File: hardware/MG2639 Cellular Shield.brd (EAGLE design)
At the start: 53.3 x 73.7 mm, 50 parts, among them J1 SIMHOLDER, Q1 MMBT2222A, Q2 MMBT2222A, U1 TXB0108, U2 SPX29302, U4 ARDUINO_R3_SHIELDNOLABELS, U5 MG2639V3

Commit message: Corrected +/- on battery connector
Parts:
- C10, C11, C3: device SparkFun:0603-CAP -> SparkFun-Capacitors:0603-CAP
- renumbered JP3 to JP5
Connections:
- net 3.8V: now also JP5.2; no longer JP5.1
- net GND: now also JP5.1; no longer JP5.2
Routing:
- net 3.8V: track 69.5 -> 71.8 mm
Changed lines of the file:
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@@
 <layer number="44" name="Drills" color="7" fill="1" visible="no" active="yes"/>
 <layer number="45" name="Holes" color="7" fill="1" visible="yes" active="yes"/>
-<layer number="46" name="Milling" color="3" fill="1" visible="yes" active="yes"/>
+<layer number="46" name="Milling" color="3" fill="1" visible="no" active="yes"/>
 <layer number="47" name="Measures" color="7" fill="1" visible="no" active="yes"/>
 <layer number="48" name="Document" color="7" fill="1" visible="no" active="yes"/>
-<layer number="49" name="Reference" color="7" fill="1" visible="yes" active="yes"/>
+<layer number="49" name="Reference" color="7" fill="1" visible="no" active="yes"/>
 <layer number="50" name="dxf" color="7" fill="1" visible="no" active="yes"/>
 <layer number="51" name="tDocu" color="6" fill="1" visible="yes" active="yes"/>
@@
 </autorouter>
 <elements>
-<element name="C3" library="SparkFun" package="0603-CAP" value="0.1uF" x="40.64" y="29.21" rot="R180"/>
+<element name="C3" library="SparkFun-Capacitors" package="0603-CAP" value="0.1uF" x="40.64" y="29.21" rot="R180">
+<attribute name="PROD_ID" value="CAP-00810" x="40.64" y="29.21" size="1.778" layer="27" rot="R180" display="off"/>
+<attribute name="VALUE" value="0.1uF" x="40.64" y="29.21" size="1.778" layer="27" rot="R180" display="off"/>
+</element>
 <element name="U$1" library="SparkFun" package="CREATIVE_COMMONS" value="CREATIVE_COMMONS" x="20.32" y="-16.51" smashed="yes"/>
 <element name="U5" library="MG2639" package="MG2639" value="MG2639V3" x="19.05" y="24.13"/>
@@
 <attribute name="PROD_ID" value="CAP-09824" x="44.45" y="20.32" size="1.778" layer="27" font="vector" ratio="15" display="off"/>
 </element>
-<element name="U2" library="SparkFun-PowerIC" package="Q5-DD_SPX29300" value="SPX29302" x="43.18" y="41.91"/>
+<element name="U2" library="SparkFun-PowerIC" package="Q5-DD_SPX29300" value="SPX29302" x="43.18" y="41.91">
+<attribute name="PROD_ID" value="VREG-08337" x="43.18" y="41.91" size="1.778" layer="27" display="off"/>
+</element>
 <element name="C2" library="SparkFun-Capacitors" package="1210" value="10uF" x="36.83" y="33.02" rot="R90">
 <attribute name="PROD_ID" value="CAP-09824" x="36.83" y="33.02" size="1.778" layer="27" font="vector" ratio="15" rot="R90" display="off"/>
@@
 <element name="LOGO1" library="SparkFun-Aesthetics" package="SFE_LOGO_NAME_FLAME_.1" value="SFE_LOGO_NAME_FLAME.1_INCH" x="24.765" y="41.275"/>
 <element name="LOGO2" library="SparkFun-Aesthetics" package="OSHW-LOGO-S" value="OSHW-LOGOS" x="35.56" y="24.003"/>
-<element name="S2" library="SparkFun-Electromechanical" package="TACTILE-SWITCH-SMD" value="BOOT" x="36.83" y="12.7" rot="R180"/>
+<element name="S2" library="SparkFun-Electromechanical" package="TACTILE-SWITCH-SMD" value="BOOT" x="36.83" y="12.7" rot="R180">
+<attribute name="PROD_ID" value="SWCH-08247" x="36.83" y="12.7" size="1.778" layer="27" rot="R180" display="off"/>
+</element>
 <element name="J1" library="SparkFun-Connectors" package="SIMHOLDER" value="SIMHOLDER" x="24.13" y="64.77" rot="R180">
 <attribute name="PROD_ID" value="CONN-08536" x="24.13" y="64.77" size="1.778" layer="27" rot="R180" display="off"/>
@@
 </element>
 <element name="SJ1" library="SparkFun-Passives" package="PAD-JUMPER-2-NC_BY_TRACE_YES_SILK" value="" x="24.13" y="45.085" rot="R90"/>
-<element name="BAT1" library="SparkFun-Electromechanical" package="BATTCON_12MM" value="20mm coincell" x="46.99" y="63.5" rot="R270"/>
+<element name="BAT1" library="SparkFun-Electromechanical" package="BATTCON_12MM" value="20mm coincell" x="46.99" y="63.5" rot="R270">
+<attribute name="PROD_ID" value="BATT-08044" x="46.99" y="63.5" size="1.778" layer="27" rot="R270" display="off"/>
+</element>
 <element name="SJ2" library="SparkFun-Passives" package="PAD-JUMPER-2-NC_BY_TRACE_YES_SILK" value="" x="22.86" y="6.35"/>
-<element name="S3" library="SparkFun-Electromechanical" package="TACTILE-SWITCH-SMD" value="BOOT" x="36.83" y="5.08"/>
+<element name="S3" library="SparkFun-Electromechanical" package="TACTILE-SWITCH-SMD" value="BOOT" x="36.83" y="5.08">
+<attribute name="PROD_ID" value="SWCH-08247" x="36.83" y="5.08" size="1.778" layer="27" display="off"/>
+</element>
 <element name="R8" library="SparkFun-Resistors" package="0603-RES" value="1K" x="17.78" y="45.72" rot="R90">
 <attribute name="PROD_ID" value="RES-07856" x="17.78" y="45.72" size="1.778" layer="27" font="vector" ratio="15" rot="R90" display="off"/>
@@
 <element name="SJ3" library="SparkFun-Passives" package="PAD-JUMPER-3-2OF3_NC_BY_PASTE_YES_SILK_FULL_BOX" value="" x="7.62" y="48.26" rot="R90"/>
 <element name="SJ4" library="SparkFun-Passives" package="PAD-JUMPER-3-2OF3_NC_BY_PASTE_YES_SILK_FULL_BOX" value="" x="7.62" y="52.07" rot="R90"/>
-<element name="U1" library="Testing" package="UFDFN-20" value="TXB0108" x="12.7" y="45.72" rot="R90"/>
+<element name="U1" library="Testing" package="UFDFN-20" value="TXB0108" x="12.7" y="45.72" rot="R90">
+<attribute name="PROD_ID" value="IC-12292" x="12.7" y="45.72" size="1.778" layer="27" rot="R90" display="off"/>
+</element>
 <element name="SJ5" library="SparkFun-Passives" package="PAD-JUMPER-3-2OF3_NC_BY_PASTE_YES_SILK_FULL_BOX" value="" x="12.7" y="49.53"/>
 <element name="JP4" library="SparkFun-Connectors" package="1X03" value="" x="2.54" y="58.42" rot="MR90"/>
 <element name="JP2" library="SparkFun-Connectors" package="1X07" value="" x="19.05" y="1.27" rot="R180"/>
-<element name="C10" library="SparkFun" package="0603-CAP" value="0.1uF" x="13.97" y="53.34" rot="R90"/>
-<element name="C11" library="SparkFun" package="0603-CAP" value="0.1uF" x="11.43" y="53.34" rot="R90"/>
+<element name="C10" library="SparkFun-Capacitors" package="0603-CAP" value="0.1uF" x="13.97" y="53.34" rot="R90">
+<attribute name="PROD_ID" value="CAP-00810" x="13.97" y="53.34" size="1.778" layer="27" rot="R90" display="off"/>
+<attribute name="VALUE" value="0.1uF" x="13.97" y="53.34" size="1.778" layer="27" rot="R90" display="off"/>
+</element>
+<element name="C11" library="SparkFun-Capacitors" package="0603-CAP" value="0.1uF" x="11.43" y="53.34" rot="R90">
+<attribute name="PROD_ID" value="CAP-00810" x="11.43" y="53.34" size="1.778" layer="27" rot="R90" display="off"/>
+<attribute name="VALUE" value="0.1uF" x="11.43" y="53.34" size="1.778" layer="27" rot="R90" display="off"/>
+</element>
 <element name="D3" library="SparkFun-LED" package="LED-1206" value="GREEN" x="20.32" y="45.72" rot="R90">
 <attribute name="PROD_ID" value="DIO-00862" x="20.32" y="45.72" size="1.778" layer="27" font="vector" ratio="15" rot="R90" display="off"/>
@@
 <attribute name="PROD_ID" value="RES-07856" x="45.72" y="29.21" size="1.778" layer="27" font="vector" ratio="15" display="off"/>
 </element>
-<element name="R2" library="SparkFun-Resistors" package="0603-RES" value="4.7K" x="25.4" y="6.35" rot="R90"/>
-<element name="R13" library="SparkFun-Resistors" package="0603-RES" value="4.7K" x="5.08" y="43.18" rot="R90"/>
+<element name="R2" library="SparkFun-Resistors" package="0603-RES" value="4.7K" x="25.4" y="6.35" rot="R90">
+<attribute name="PROD_ID" value="RES-07857" x="25.4" y="6.35" size="1.778" layer="27" rot="R90" display="off"/>
+<attribute name="VALUE" value="4.7K" x="25.4" y="6.35" size="1.778" layer="27" rot="R90" display="off"/>
+</element>
+<element name="R13" library="SparkFun-Resistors" package="0603-RES" value="4.7K" x="5.08" y="43.18" rot="R90">
+<attribute name="PROD_ID" value="RES-07857" x="5.08" y="43.18" size="1.778" layer="27" rot="R90" display="off"/>
+<attribute name="VALUE" value="4.7K" x="5.08" y="43.18" size="1.778" layer="27" rot="R90" display="off"/>
+</element>
 <element name="U$2" library="SparkFun-RF" package="SMA_BULKHEAD" value="SMA_HOLE" x="40.767" y="53.975"/>
 <element name="LOGO3" library="SparkFun-Aesthetics" package="SFE_LOGO_NAME_FLAME_.2" value="SFE_LOGO_NAME_FLAME.2_INCH" x="38.481" y="33.528" rot="MR0"/>
 <element name="SJ6" library="SparkFun-Passives" package="PAD-JUMPER-2-NC_BY_TRACE_YES_SILK" value="" x="43.18" y="29.21" rot="R270"/>
-<element name="JP3" library="SparkFun-Connectors" package="JST-2-PTH" value="LiPo" x="46.99" y="12.7" rot="R270">
-<attribute name="SKU" value="PRT-09914" x="46.99" y="12.7" size="1.016" layer="27" font="vector" ratio="15" rot="R270" display="off"/>
+<element name="JP5" library="SparkFun-Connectors" package="JST-2-PTH" value="LiPo" x="46.99" y="12.7" rot="R270">
+<attribute name="SKU" value="PRT-09914" x="46.99" y="12.7" size="1.778" layer="27" font="vector" ratio="15" rot="R270" display="off"/>
 </element>
 </elements>
@@
 <via x="21.082" y="40.64" extent="1-16" drill="0.508"/>
 <via x="20.32" y="35.56" extent="1-16" drill="0.508"/>
-<contactref element="JP3" pad="2"/>
+<contactref element="JP5" pad="1"/>
 </signal>
 <signal name="SIM_CLK">
@@
 <wire x1="35.56" y1="25.4" x2="34.29" y2="26.67" width="0.4572" layer="1"/>
 <contactref element="SJ6" pad="2"/>
-<contactref element="JP3" pad="1"/>
 <wire x1="43.18" y1="28.702" x2="43.18" y2="28.067" width="0.4572" layer="1"/>
 <wire x1="43.18" y1="28.067" x2="42.545" y2="27.432" width="0.4572" layer="1"/>
@@
 <wire x1="41.49" y1="27.471" x2="41.529" y2="27.432" width="0.4572" layer="1"/>
 <wire x1="42.85" y1="20.32" x2="42.85" y2="16.84" width="0.4572" layer="1"/>
-<wire x1="42.85" y1="16.84" x2="45.99" y2="13.7" width="0.4572" layer="1"/>
-<wire x1="46.99" y1="13.7" x2="45.99" y2="13.7" width="0.4572" layer="1"/>
+<contactref element="JP5" pad="2"/>
+<wire x1="42.85" y1="16.84" x2="44.45" y2="15.24" width="0.4572" layer="1"/>
+<wire x1="44.45" y1="15.24" x2="44.45" y2="12.7" width="0.4572" layer="1"/>
+<wire x1="46.99" y1="11.7" x2="45.45" y2="11.7" width="0.4572" layer="1"/>
+<wire x1="45.45" y1="11.7" x2="44.45" y2="12.7" width="0.4572" layer="1"/>
 </signal>
 <signal name="N$2">

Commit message: Prelim firmware. Works for certain features.
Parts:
- BAT1: value 20mm coincell -> 12mm coincell
- D2: value RED -> BLUE
- U4: value ARDUINO_R3_SHIELDNOLABELS -> ARDUINO_R3_SHIELD
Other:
- board text added: "+"
- board text added: "BATT"
- board text added: "N. Seidle"
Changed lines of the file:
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@@
 <layer number="37" name="tTest" color="7" fill="1" visible="no" active="yes"/>
 <layer number="38" name="bTest" color="7" fill="1" visible="no" active="yes"/>
-<layer number="39" name="tKeepout" color="4" fill="11" visible="no" active="yes"/>
-<layer number="40" name="bKeepout" color="1" fill="11" visible="no" active="yes"/>
+<layer number="39" name="tKeepout" color="4" fill="11" visible="yes" active="yes"/>
+<layer number="40" name="bKeepout" color="1" fill="11" visible="yes" active="yes"/>
 <layer number="41" name="tRestrict" color="4" fill="10" visible="no" active="yes"/>
 <layer number="42" name="bRestrict" color="1" fill="10" visible="no" active="yes"/>
@@
 <layer number="47" name="Measures" color="7" fill="1" visible="no" active="yes"/>
 <layer number="48" name="Document" color="7" fill="1" visible="no" active="yes"/>
-<layer number="49" name="Reference" color="7" fill="1" visible="no" active="yes"/>
+<layer number="49" name="Reference" color="7" fill="1" visible="yes" active="yes"/>
 <layer number="50" name="dxf" color="7" fill="1" visible="no" active="yes"/>
 <layer number="51" name="tDocu" color="6" fill="1" visible="yes" active="yes"/>
@@
 Batt</text>
 <text x="48.641" y="28.194" size="1.016" layer="21" font="vector" ratio="15" rot="R90">SJ6</text>
+<text x="48.387" y="10.795" size="1.778" layer="21" font="vector" ratio="15">+</text>
+<text x="48.387" y="12.827" size="1.778" layer="21" font="vector" ratio="15">-</text>
+<text x="46.99" y="16.002" size="1.27" layer="21" font="vector" ratio="15">BATT</text>
+<text x="52.07" y="-16.51" size="1.778" layer="27" font="vector" ratio="15">N. Seidle</text>
 </plain>
 <attributes>
@@
 <attribute name="PROD_ID" value="CAP-07890" x="43.18" y="25.4" size="1.778" layer="27" font="vector" ratio="15" rot="R180" display="off"/>
 </element>
-<element name="U4" library="SparkFun-Boards" package="UNO_R3_SHIELD_NOLABELS" value="ARDUINO_R3_SHIELDNOLABELS" x="0" y="0"/>
+<element name="U4" library="SparkFun-Boards" package="UNO_R3_SHIELD_NOLABELS" value="ARDUINO_R3_SHIELD" x="0" y="0"/>
 <element name="Q1" library="SparkFun-DiscreteSemi" package="SOT23-3" value="MMBT2222A" x="27.94" y="6.35" rot="R270">
 <attribute name="PROD_ID" value="TRANS-08049" x="27.94" y="6.35" size="1.778" layer="27" rot="R270" display="off"/>
@@
 </element>
 <element name="SJ1" library="SparkFun-Passives" package="PAD-JUMPER-2-NC_BY_TRACE_YES_SILK" value="" x="24.13" y="45.085" rot="R90"/>
-<element name="BAT1" library="SparkFun-Electromechanical" package="BATTCON_12MM" value="20mm coincell" x="46.99" y="63.5" rot="R270">
+<element name="BAT1" library="SparkFun-Electromechanical" package="BATTCON_12MM" value="12mm coincell" x="46.99" y="63.5" rot="R270">
 <attribute name="PROD_ID" value="BATT-08044" x="46.99" y="63.5" size="1.778" layer="27" rot="R270" display="off"/>
 </element>
@@
 <attribute name="PROD_ID" value="RES-07856" x="17.78" y="45.72" size="1.778" layer="27" font="vector" ratio="15" rot="R90" display="off"/>
 </element>
-<element name="D2" library="SparkFun-LED" package="LED-1206" value="RED" x="2.54" y="6.35" rot="R270">
-<attribute name="PROD_ID" value="DIO-00809" x="2.54" y="6.35" size="1.778" layer="27" font="vector" ratio="15" rot="R270" display="off"/>
+<element name="D2" library="SparkFun-LED" package="LED-1206" value="BLUE" x="2.54" y="6.35" rot="R270">
+<attribute name="PROD_ID" value="DIO-09911" x="2.54" y="6.35" size="1.778" layer="27" font="vector" ratio="15" rot="R270" display="off"/>
 </element>
 <element name="R9" library="SparkFun-Resistors" package="0603-RES" value="1K" x="5.08" y="10.16" rot="R270">

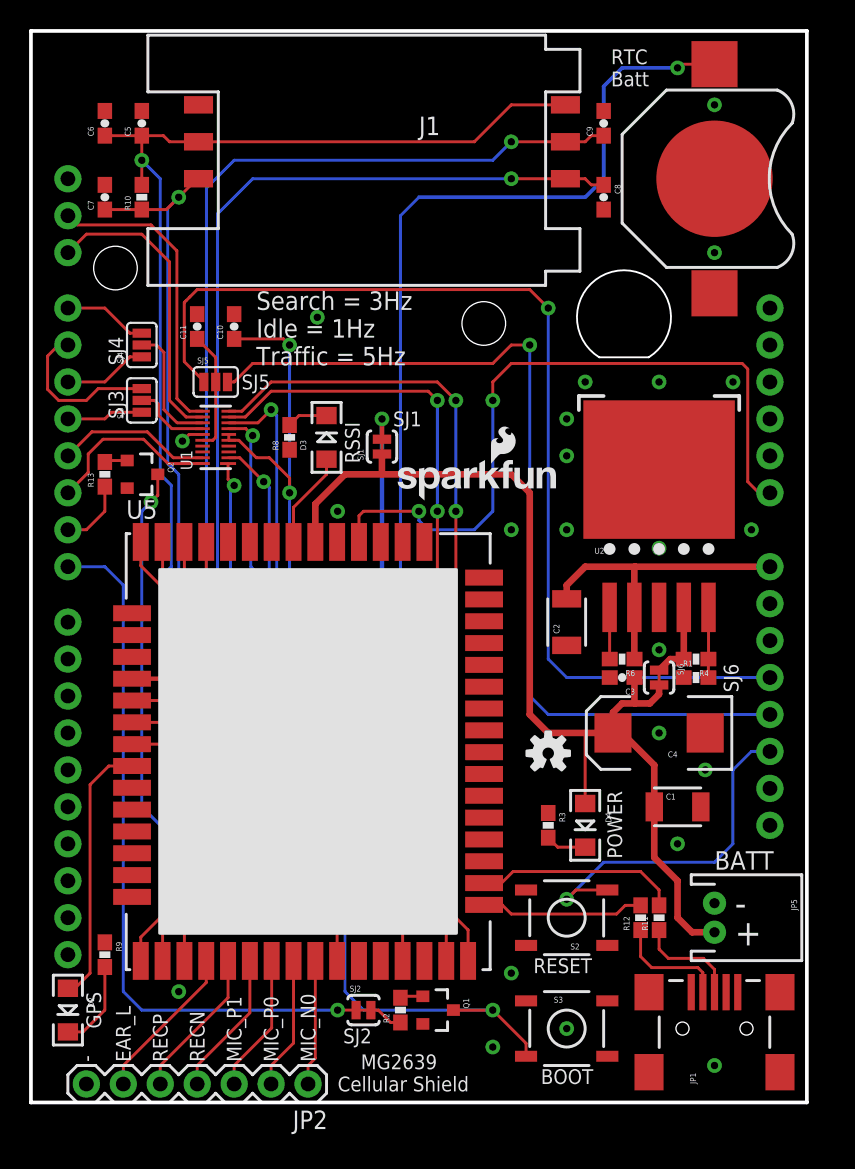
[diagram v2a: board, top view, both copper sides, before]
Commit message: Add silk labels to pins/jumpers. Add FTDI header. Remove SYSRST circuit. Reconfiguring jumpers. Removed USB connector, broke USB pins out to headers.
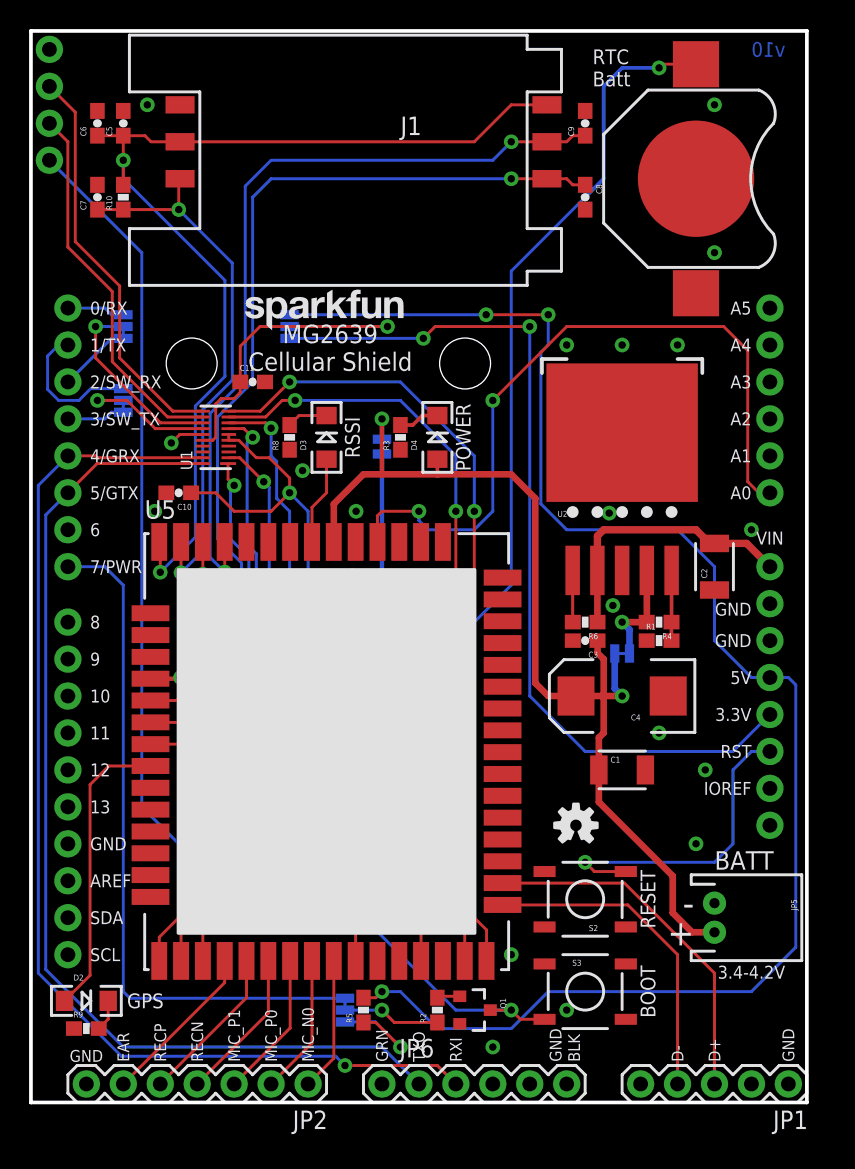
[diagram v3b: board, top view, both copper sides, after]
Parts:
- removed LOGO1: SFE_LOGO_NAME_FLAME.1_INCH, SparkFun-Aesthetics:SFE_LOGO_NAME_FLAME_.1
- removed Q2: MMBT2222A, SparkFun-DiscreteSemi:SOT23-3
- removed R11, R12: 22, SparkFun-Resistors:0603-RES
- removed R13: 4.7K, SparkFun-Resistors:0603-RES
- removed U$1: CREATIVE_COMMONS, SparkFun:CREATIVE_COMMONS
- removed U$2: SMA_HOLE, SparkFun-RF:SMA_BULKHEAD
- added FRAME1: FRAME-LEDGER, SparkFun-Aesthetics:CREATIVE_COMMONS
- added JP3: M01PTH, SparkFun-Connectors:1X01
- added JP6: FTDI_BASICPTH, SparkFun-Connectors:FTDI_BASIC
- added LOGO4: SFE_LOGO_NAME.1_INCH, SparkFun-Aesthetics:SFE_LOGO_NAME_.1
- added R5: 1K, SparkFun-Resistors:0603-RES
- JP1: value USBSMD -> (none); device SparkFun-Connectors:USB-MINIB -> SparkFun-Connectors:1X05
- JP2: value (none) -> AUDIO
- S2: value BOOT -> RESET
- SJ2: device SparkFun-Passives:PAD-JUMPER-2-NC_BY_TRACE_YES_SILK -> SparkFun-Passives:PAD-JUMPER-3-2OF3_NC_BY_TRACE_YES_SILK_FULL_BOX
- SJ3, SJ4, SJ5: device SparkFun-Passives:PAD-JUMPER-3-2OF3_NC_BY_PASTE_YES_SILK_FULL_BOX -> SparkFun-Passives:PAD-JUMPER-3-2OF3_NC_BY_TRACE_YES_SILK_FULL_BOX
- moved D4 28.5 mm to (27.9, 45.7), turned to 90 degrees
- moved R3 28.5 mm to (25.4, 45.7), turned to 90 degrees
- moved C10 12.0 mm to (10.2, 41.9), turned to 180 degrees
- moved C2 10.9 mm to (47.0, 36.8)
- moved JP4 8.98 mm to (1.27, 67.3)
- moved SJ5 6.35 mm to (17.8, 53.3), flipped to the bottom, turned to 270 degrees
- moved JP1 6.35 mm to (52.1, 1.27), turned to 180 degrees
- moved C11 5.39 mm to (15.2, 49.5), turned to 0 degrees
- moved LOGO2 5.31 mm to (37.5, 19.1)
- moved R9 5.24 mm to (3.81, 5.08), turned to 0 degrees
- moved C1 4.58 mm to (40.6, 22.9)
- moved U2 3.59 mm to (40.6, 44.5)
- moved C4 3.59 mm to (40.6, 27.9)
- moved R4 3.59 mm to (43.2, 33.0)
- moved R6 3.59 mm to (38.1, 33.0)
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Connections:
- removed net N$10: JP1.D+, R11.1
- removed net N$11: JP1.D-, R12.1
- removed net N$2: Q2.1, R13.2
- new net N$6: R5.1, SJ2.1
- net !SYSRST: now also JP3.1; no longer Q2.3
- net 5V: now also R5.2
- net CELL_RESET: no longer R13.1
- net GND: now also JP1.1, JP6.GND; no longer JP1.GND, Q2.2
- net GRX-HV: now also JP6.TXO
- net GTX-HV: now also JP6.RXI
- net ON/OFF: now also SJ2.3; no longer SJ2.1
- net RX-SOFT: now also SJ4.3; no longer SJ4.1
- net RXI: now also SJ4.1; no longer SJ4.3
- net TX-SOFT: now also SJ3.3; no longer SJ3.1
- net TXO: now also SJ3.1; no longer SJ3.3
- net USB+: now also JP1.3; no longer R11.2
- net USB-: now also JP1.4; no longer R12.2
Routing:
- net GRX-HV: track 10.7 -> 77.6 mm, vias 0 -> 1
- net GTX-HV: track 12.2 -> 72.4 mm
- net 5V: track 71.8 -> 107.9 mm, vias 1 -> 3
- net !SYSRST: track 35.8 -> 59.4 mm, vias 2 -> 1
- net VCCB: track 8.28 -> 25.9 mm, vias 0 -> 1
- net USB-: track 11.3 -> 22.3 mm
- net USB+: track 13.9 -> 24.8 mm
- net GPS_RTC: track 82.5 -> 73.2 mm
- net N$6: track 0.00 -> 8.36 mm, vias 0 -> 1
- net N$11: track 7.90 -> 0.00 mm
- net SIM_RST: track 62.1 -> 54.8 mm
- net N$10: track 7.26 -> 0.00 mm
- net TX2-HV: track 20.8 -> 27.9 mm
- net SIM_CLK: track 63.9 -> 56.9 mm
- net !PWRKEY: track 25.8 -> 20.0 mm
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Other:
- board text added: "0/RX"
- board text added: "1/TX"
- board text added: "10"
- board text added: "11"
- board text added: "12"
- board text added: "13"
- board text added: "2/SW_RX"
- board text added: "3.3V"
- board text added: "3.4-4.2V"
- board text added: "3.8V"
- board text added: "3/SW_TX"
- board text added: "4/GRX"
- board text added: "5/GTX"
- board text added: "5V"
- board text added: "6"
- board text added: "7/PWR"
- board text added: "8"
- board text added: "9"
- board text added: "A0"
- board text added: "A1"
- board text added: "A2"
- board text added: "A3"
- board text added: "A4"
- board text added: "A5"
- board text added: "AREF"
- board text added: "BLK"
- board text added: "D+"
- board text added: "D-"
- board text added: "D6"
- board text added: "EAR"
- board text added: "GRN"
- board text added: "HW/0"
- board text added: "HW/1"
- board text added: "IOREF"
- board text added: "Nathan Seidle Jim Lindblom"
- board text added: "RST"
- board text added: "RX"
- board text added: "RXI"
- board text added: "SCL"
- board text added: "SDA"
- board text added: "SW/2"
- board text added: "SW/3"
- board text added: "TX"
- board text added: "TXO"
- board text added: "VBAT"
- board text added: "VDDIO"
- board text added: "VGPS"
- board text added: "VIN"
- board text added: "v10"
- board text removed: "EAR_L"
- board text removed: "SJ2"
- board text removed: "SJ3"
- board text removed: "SJ4"
- board text removed: "SJ5"
- board text removed: "Search = 3Hz Idle = 1Hz Traffic = 5Hz"
